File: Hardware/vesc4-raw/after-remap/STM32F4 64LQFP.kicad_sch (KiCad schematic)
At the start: 15 parts, among them P2 SWD, U1 STM32F40X_LQFP64, X2 8MHz 10ppm

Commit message: export footprint & ngapus warning unmatched
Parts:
- C10: symbol after-remap-rescue:C-RESCUE-BLDC_4 -> vesc4-legacy:C-RESCUE-BLDC_4_17
- C11: symbol after-remap-rescue:C-RESCUE-BLDC_4 -> vesc4-legacy:C-RESCUE-BLDC_4_16
- C12: symbol after-remap-rescue:C-RESCUE-BLDC_4 -> vesc4-legacy:C-RESCUE-BLDC_4_18
- C13: symbol after-remap-rescue:C-RESCUE-BLDC_4 -> vesc4-legacy:C-RESCUE-BLDC_4_20
- C14: symbol after-remap-rescue:C-RESCUE-BLDC_4 -> vesc4-legacy:C-RESCUE-BLDC_4_19
- C15: symbol after-remap-rescue:C-RESCUE-BLDC_4 -> vesc4-legacy:C-RESCUE-BLDC_4_13
- C16: symbol after-remap-rescue:C-RESCUE-BLDC_4 -> vesc4-legacy:C-RESCUE-BLDC_4_21
- C17: symbol after-remap-rescue:C-RESCUE-BLDC_4 -> vesc4-legacy:C-RESCUE-BLDC_4_24
- C31: symbol after-remap-rescue:C-RESCUE-BLDC_4 -> vesc4-legacy:C-RESCUE-BLDC_4_22
- C32: symbol after-remap-rescue:C-RESCUE-BLDC_4 -> vesc4-legacy:C-RESCUE-BLDC_4_14
- C35: symbol after-remap-rescue:C-RESCUE-BLDC_4 -> vesc4-legacy:C-RESCUE-BLDC_4_23
- C38: symbol after-remap-rescue:C-RESCUE-BLDC_4 -> vesc4-legacy:C-RESCUE-BLDC_4_15
- P2: symbol after-remap-rescue:CONN_6 -> vesc4-legacy:CONN_6_2
- U1: symbol after-remap-rescue:STM32F40X_LQFP64 -> vesc4-legacy:STM32F40X_LQFP64_2
- X2: symbol after-remap-rescue:CRYSTAL_SMD -> vesc4-legacy:CRYSTAL_SMD_2
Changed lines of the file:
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@@
 	(symbol
 		(lib_name "STM32F40X_LQFP64_2")
-		(lib_id "after-remap-rescue:STM32F40X_LQFP64")
+		(lib_id "vesc4-legacy:STM32F40X_LQFP64_2")
 		(at 146.05 99.06 0)
 		(unit 1)
@@
 	(symbol
 		(lib_name "C-RESCUE-BLDC_4_24")
-		(lib_id "after-remap-rescue:C-RESCUE-BLDC_4")
+		(lib_id "vesc4-legacy:C-RESCUE-BLDC_4_24")
 		(at 190.5 161.29 90)
 		(unit 1)
@@
 	(symbol
 		(lib_name "C-RESCUE-BLDC_4_21")
-		(lib_id "after-remap-rescue:C-RESCUE-BLDC_4")
+		(lib_id "vesc4-legacy:C-RESCUE-BLDC_4_21")
 		(at 190.5 154.94 90)
 		(unit 1)
@@
 	(symbol
 		(lib_name "GND-RESCUE-BLDC_4_15")
-		(lib_id "after-remap-rescue:GND-RESCUE-BLDC_4")
+		(lib_id "vesc4-legacy:GND-RESCUE-BLDC_4_15")
 		(at 203.2 153.67 0)
 		(unit 1)
@@
 	(symbol
 		(lib_name "VCC_9")
-		(lib_id "after-remap-rescue:VCC")
+		(lib_id "vesc4-legacy:VCC_9")
 		(at 187.96 129.54 0)
 		(unit 1)
@@
 	(symbol
 		(lib_name "GND-RESCUE-BLDC_4_14")
-		(lib_id "after-remap-rescue:GND-RESCUE-BLDC_4")
+		(lib_id "vesc4-legacy:GND-RESCUE-BLDC_4_14")
 		(at 182.88 130.81 0)
 		(unit 1)
@@
 	(symbol
 		(lib_name "VCC_6")
-		(lib_id "after-remap-rescue:VCC")
+		(lib_id "vesc4-legacy:VCC_6")
 		(at 182.88 106.68 0)
 		(unit 1)
@@
 	(symbol
 		(lib_name "C-RESCUE-BLDC_4_13")
-		(lib_id "after-remap-rescue:C-RESCUE-BLDC_4")
+		(lib_id "vesc4-legacy:C-RESCUE-BLDC_4_13")
 		(at 186.69 45.72 180)
 		(unit 1)
@@
 	(symbol
 		(lib_name "C-RESCUE-BLDC_4_15")
-		(lib_id "after-remap-rescue:C-RESCUE-BLDC_4")
+		(lib_id "vesc4-legacy:C-RESCUE-BLDC_4_15")
 		(at 205.74 45.72 180)
 		(unit 1)
@@
 	(symbol
 		(lib_name "GND-RESCUE-BLDC_4_10")
-		(lib_id "after-remap-rescue:GND-RESCUE-BLDC_4")
+		(lib_id "vesc4-legacy:GND-RESCUE-BLDC_4_10")
 		(at 209.55 40.64 0)
 		(unit 1)
@@
 	(symbol
 		(lib_name "GND-RESCUE-BLDC_4_12")
-		(lib_id "after-remap-rescue:GND-RESCUE-BLDC_4")
+		(lib_id "vesc4-legacy:GND-RESCUE-BLDC_4_12")
 		(at 181.61 64.77 0)
 		(unit 1)
@@
 	(symbol
 		(lib_name "C-RESCUE-BLDC_4_22")
-		(lib_id "after-remap-rescue:C-RESCUE-BLDC_4")
+		(lib_id "vesc4-legacy:C-RESCUE-BLDC_4_22")
 		(at 196.85 138.43 180)
 		(unit 1)
@@
 	(symbol
 		(lib_name "C-RESCUE-BLDC_4_23")
-		(lib_id "after-remap-rescue:C-RESCUE-BLDC_4")
+		(lib_id "vesc4-legacy:C-RESCUE-BLDC_4_23")
 		(at 203.2 138.43 180)
 		(unit 1)
@@
 	(symbol
 		(lib_name "VCC_8")
-		(lib_id "after-remap-rescue:VCC")
+		(lib_id "vesc4-legacy:VCC_8")
 		(at 182.88 135.89 0)
 		(unit 1)
@@
 	(symbol
 		(lib_name "GND-RESCUE-BLDC_4_11")
-		(lib_id "after-remap-rescue:GND-RESCUE-BLDC_4")
+		(lib_id "vesc4-legacy:GND-RESCUE-BLDC_4_11")
 		(at 201.93 83.82 0)
 		(unit 1)
@@
 	(symbol
 		(lib_name "C-RESCUE-BLDC_4_14")
-		(lib_id "after-remap-rescue:C-RESCUE-BLDC_4")
+		(lib_id "vesc4-legacy:C-RESCUE-BLDC_4_14")
 		(at 201.93 78.74 180)
 		(unit 1)
@@
 	(symbol
 		(lib_name "CONN_6_2")
-		(lib_id "after-remap-rescue:CONN_6")
+		(lib_id "vesc4-legacy:CONN_6_2")
 		(at 256.54 80.01 0)
 		(unit 1)
@@
 	(symbol
 		(lib_name "VCC_10")
-		(lib_id "after-remap-rescue:VCC")
+		(lib_id "vesc4-legacy:VCC_10")
 		(at 251.46 69.85 270)
 		(unit 1)
@@
 	(symbol
 		(lib_name "GND-RESCUE-BLDC_4_16")
-		(lib_id "after-remap-rescue:GND-RESCUE-BLDC_4")
+		(lib_id "vesc4-legacy:GND-RESCUE-BLDC_4_16")
 		(at 243.84 78.74 270)
 		(unit 1)
@@
 	(symbol
 		(lib_name "C-RESCUE-BLDC_4_17")
-		(lib_id "after-remap-rescue:C-RESCUE-BLDC_4")
+		(lib_id "vesc4-legacy:C-RESCUE-BLDC_4_17")
 		(at 238.76 33.02 180)
 		(unit 1)
@@
 	(symbol
 		(lib_name "C-RESCUE-BLDC_4_16")
-		(lib_id "after-remap-rescue:C-RESCUE-BLDC_4")
+		(lib_id "vesc4-legacy:C-RESCUE-BLDC_4_16")
 		(at 245.11 33.02 180)
 		(unit 1)
@@
 	(symbol
 		(lib_name "C-RESCUE-BLDC_4_19")
-		(lib_id "after-remap-rescue:C-RESCUE-BLDC_4")
+		(lib_id "vesc4-legacy:C-RESCUE-BLDC_4_19")
 		(at 264.16 33.02 180)
 		(unit 1)
@@
 	(symbol
 		(lib_name "GND-RESCUE-BLDC_4_13")
-		(lib_id "after-remap-rescue:GND-RESCUE-BLDC_4")
+		(lib_id "vesc4-legacy:GND-RESCUE-BLDC_4_13")
 		(at 231.14 41.91 0)
 		(unit 1)
@@
 	(symbol
 		(lib_name "VCC_7")
-		(lib_id "after-remap-rescue:VCC")
+		(lib_id "vesc4-legacy:VCC_7")
 		(at 231.14 24.13 0)
 		(unit 1)
@@
 	(symbol
 		(lib_name "C-RESCUE-BLDC_4_18")
-		(lib_id "after-remap-rescue:C-RESCUE-BLDC_4")
+		(lib_id "vesc4-legacy:C-RESCUE-BLDC_4_18")
 		(at 251.46 33.02 180)
 		(unit 1)
@@
 	(symbol
 		(lib_name "C-RESCUE-BLDC_4_20")
-		(lib_id "after-remap-rescue:C-RESCUE-BLDC_4")
+		(lib_id "vesc4-legacy:C-RESCUE-BLDC_4_20")
 		(at 257.81 33.02 180)
 		(unit 1)
@@
 	(symbol
 		(lib_name "CRYSTAL_SMD_2")
-		(lib_id "after-remap-rescue:CRYSTAL_SMD")
+		(lib_id "vesc4-legacy:CRYSTAL_SMD_2")
 		(at 196.85 52.07 0)
 		(unit 1)
@@
 	(symbol
 		(lib_name "GND-RESCUE-BLDC_4_9")
-		(lib_id "after-remap-rescue:GND-RESCUE-BLDC_4")
+		(lib_id "vesc4-legacy:GND-RESCUE-BLDC_4_9")
 		(at 196.85 54.61 0)
 		(unit 1)

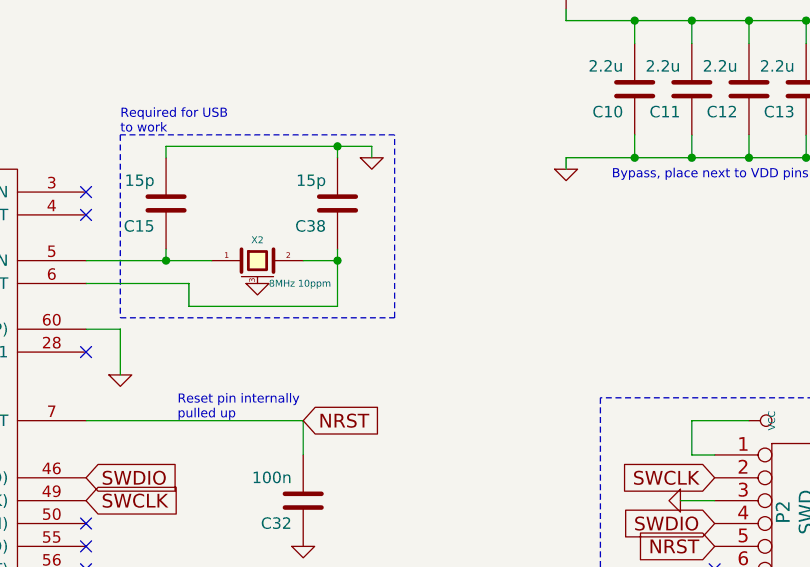
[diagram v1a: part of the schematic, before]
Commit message: changed crystal x2
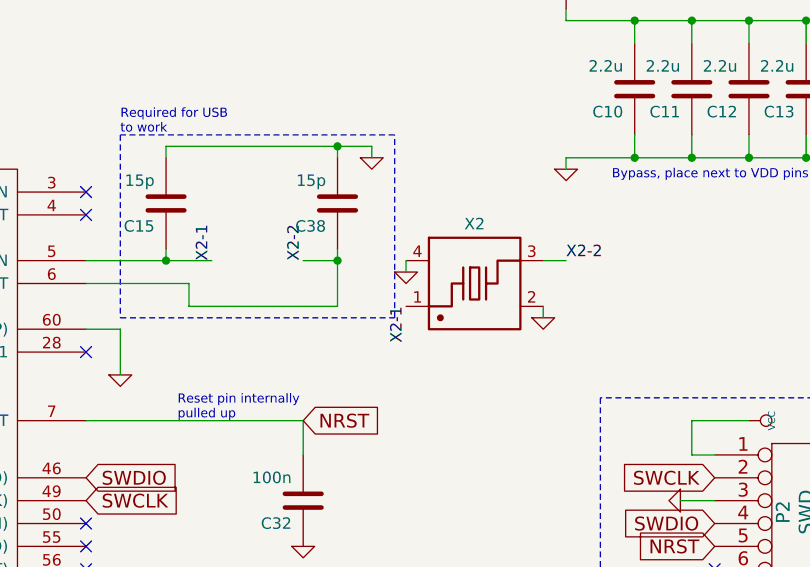
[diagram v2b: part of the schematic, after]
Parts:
- removed X2: 8MHz 10ppm, CRF1:Crystal_5x3mm, symbol vesc4-legacy:CRYSTAL_SMD_2
- added X2: 5TJ480000NYLBC, Library:C2149245, symbol Library:5TJ480000NYLBC
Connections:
- net GND: now also X2.2 (GND), X2.4 (GND)
- net X2-1: now reaches C15.1, U1.5 (PH0-OSC_IN)
- net X2-1: now also X2.1
- net X2-2: now reaches C38.1, U1.6 (PH1-OSC_OUT)
- net X2-2: now also X2.3
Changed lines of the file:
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@@
 		)
 	)
+	(wire
+		(pts
+			(xy 228.6 52.07) (xy 231.14 52.07)
+		)
+		(stroke
+			(width 0)
+			(type default)
+		)
+	)
 	(polyline
 		(pts
@@
 	(wire
 		(pts
+			(xy 228.6 57.15) (xy 228.6 58.42)
+		)
+		(stroke
+			(width 0)
+			(type default)
+		)
+	)
+	(wire
+		(pts
 			(xy 196.85 146.05) (xy 203.2 146.05)
 		)
@@
 	(wire
 		(pts
+			(xy 213.36 53.34) (xy 213.36 52.07)
+		)
+		(stroke
+			(width 0)
+			(type default)
+		)
+	)
+	(wire
+		(pts
 			(xy 182.88 110.49) (xy 182.88 113.03)
 		)
@@
 		)
 	)
+	(label "X2-1"
+		(at 213.36 57.15 270)
+		(effects
+			(font
+				(size 1.27 1.27)
+			)
+			(justify right bottom)
+		)
+	)
+	(label "X2-1"
+		(at 191.77 52.07 90)
+		(effects
+			(font
+				(size 1.27 1.27)
+			)
+			(justify left bottom)
+		)
+	)
+	(label "X2-2"
+		(at 201.93 52.07 90)
+		(effects
+			(font
+				(size 1.27 1.27)
+			)
+			(justify left bottom)
+		)
+	)
+	(label "X2-2"
+		(at 231.14 52.07 0)
+		(effects
+			(font
+				(size 1.27 1.27)
+			)
+			(justify left bottom)
+		)
+	)
 	(global_label "SWCLK"
 		(shape input)
@@
 	)
 	(symbol
-		(lib_name "CRYSTAL_SMD_2")
-		(lib_id "vesc4-legacy:CRYSTAL_SMD_2")
-		(at 196.85 52.07 0)
+		(lib_name "GND-RESCUE-BLDC_4_9")
+		(lib_id "vesc4-legacy:GND-RESCUE-BLDC_4_9")
+		(at 213.36 53.34 0)
 		(unit 1)
 		(exclude_from_sim no)
@@
 		(on_board yes)
 		(dnp no)
-		(property "Reference" "X2"
-			(at 196.85 49.784 0)
+		(property "Reference" "#PWR063"
+			(at 213.36 53.34 0)
 			(effects
 				(font
 					(size 0.762 0.762)
 				)
+				(hide yes)
 			)
 		)
-		(property "Value" "8MHz 10ppm"
-			(at 198.12 54.61 0)
+		(property "Value" "GND"
+			(at 213.36 55.118 0)
 			(effects
 				(font
 					(size 0.762 0.762)
 				)
-				(justify left)
+				(hide yes)
 			)
 		)
-		(property "Footprint" "CRF1:Crystal_5x3mm"
-			(at 196.85 52.07 0)
+		(property "Footprint" ""
+			(at 213.36 53.34 0)
 			(effects
 				(font
@@
 		)
 		(property "Datasheet" ""
-			(at 196.85 52.07 0)
+			(at 213.36 53.34 0)
 			(effects
 				(font
 					(size 1.524 1.524)
 				)
+				(hide yes)
+			)
+		)
+		(property "Description" ""
+			(at 213.36 53.34 0)
+			(effects
+				(font
+					(size 1.27 1.27)
+				)
+			)
+		)
+		(pin "1"
+		)
+		(instances
+			(project "after-remap"
+				(path "/97cdaedc-7981-4798-95b0-56b9c66aae09/00000000-0000-0000-0000-000053f7501a"
+					(reference "#PWR063")
+					(unit 1)
+				)
+			)
+		)
+	)
+	(symbol
+		(lib_id "Library:5TJ480000NYLBC")
+		(at 220.98 54.61 0)
+		(unit 1)
+		(exclude_from_sim no)
+		(in_bom yes)
+		(on_board yes)
+		(dnp no)
+		(property "Reference" "X2"
+			(at 220.98 48.006 0)
+			(effects
+				(font
+					(size 1.27 1.27)
+				)
+			)
+		)
+		(property "Value" "5TJ480000NYLBC"
+			(at 220.98 46.99 0)
+			(effects
+				(font
+					(size 1.27 1.27)
+				)
+				(hide yes)
+			)
+		)
+		(property "Footprint" "Library:C2149245"
+			(at 220.98 54.61 0)
+			(effects
+				(font
+					(size 1.27 1.27)
+				)
+				(hide yes)
+			)
+		)
+		(property "Datasheet" ""
+			(at 220.98 54.61 0)
+			(effects
+				(font
+					(size 1.27 1.27)
+				)
+				(hide yes)
 			)
 		)
 		(property "Description" ""
-			(at 196.85 52.07 0)
+			(at 220.98 54.61 0)
 			(effects
 				(font
 					(size 1.27 1.27)
 				)
+				(hide yes)
 			)
 		)
-		(property "mfg#" "ABM3B-8.0-10-1UT"
-			(at 196.85 52.07 0)
+		(property "Manufacturer Part" "5TJ480000NYLBC"
+			(at 220.98 54.61 0)
 			(effects
 				(font
-					(size 1.524 1.524)
+					(size 1.27 1.27)
+				)
+				(hide yes)
+			)
+		)
+		(property "Manufacturer" "JYJE(晶友嘉)"
+			(at 220.98 54.61 0)
+			(effects
+				(font
+					(size 1.27 1.27)
+				)
+				(hide yes)
+			)
+		)
+		(property "Supplier Part" "C2149245"
+			(at 220.98 54.61 0)
+			(effects
+				(font
+					(size 1.27 1.27)
+				)
+				(hide yes)
+			)
+		)
+		(property "Supplier" "LCSC"
+			(at 220.98 54.61 0)
+			(effects
+				(font
+					(size 1.27 1.27)
 				)
 				(hide yes)
@@
 		(pin "1"
 		)
+		(pin "3"
+		)
 		(pin "2"
 		)
-		(pin "3"
+		(pin "4"
 		)
 		(instances
-			(project "after-remap"
+			(project ""
 				(path "/97cdaedc-7981-4798-95b0-56b9c66aae09/00000000-0000-0000-0000-000053f7501a"
 					(reference "X2")
@@
 		(lib_name "GND-RESCUE-BLDC_4_9")
 		(lib_id "vesc4-legacy:GND-RESCUE-BLDC_4_9")
-		(at 196.85 54.61 0)
+		(at 228.6 58.42 0)
 		(unit 1)
 		(exclude_from_sim no)
@@
 		(on_board yes)
 		(dnp no)
-		(property "Reference" "#PWR047"
-			(at 196.85 54.61 0)
+		(property "Reference" "#PWR064"
+			(at 228.6 58.42 0)
 			(effects
 				(font
@@
 		)
 		(property "Value" "GND"
-			(at 196.85 56.388 0)
+			(at 228.6 60.198 0)
 			(effects
 				(font
@@
 		)
 		(property "Footprint" ""
-			(at 196.85 54.61 0)
+			(at 228.6 58.42 0)
 			(effects
 				(font
@@
 		)
 		(property "Datasheet" ""
-			(at 196.85 54.61 0)
+			(at 228.6 58.42 0)
 			(effects
 				(font
@@
 		)
 		(property "Description" ""
-			(at 196.85 54.61 0)
+			(at 228.6 58.42 0)
 			(effects
 				(font
@@
 			(project "after-remap"
 				(path "/97cdaedc-7981-4798-95b0-56b9c66aae09/00000000-0000-0000-0000-000053f7501a"
-					(reference "#PWR047")
+					(reference "#PWR064")
 					(unit 1)
 				)
